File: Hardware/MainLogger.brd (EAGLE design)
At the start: 98.9 x 72.1 mm, 247 parts, among them J3 GEMS_POWER_PLUGINPUT_RT, J4 U.FL, J5 B_SERIES_M.2EKEY_3042, P1:C1 0.1uF, P1:C2 2.2uF, P1:C3 1uF, P1:C4 100uF, P1:C5 0.1uF, P1:J1 CONN_TALON_LOGGER, P1:R1 100k, P1:U1 SN74AUP1G08DCK, P1:U2 FXMAR2102UMLP, P1:U3 FSA2258, P1:U4 AP2411, P2:C1 0.1uF, P2:C2 2.2uF, P2:C3 1uF, P2:C4 100uF, P2:C5 0.1uF, P2:J1 CONN_TALON_LOGGER, P2:R1 100k, P2:U1 SN74AUP1G08DCK, P2:U2 FXMAR2102UMLP, P2:U3 FSA2258, P2:U4 AP2411, P3:C1 0.1uF, P3:C2 2.2uF, P3:C3 1uF, P3:C4 100uF, P3:C5 0.1uF, P3:J1 CONN_TALON_LOGGER, P3:R1 100k, P3:U1 SN74AUP1G08DCK, P3:U2 FXMAR2102UMLP, P3:U3 FSA2258, P3:U4 AP2411, P4:C1 0.1uF, P4:C2 2.2uF, P4:C3 1uF, P4:C4 100uF, P4:C5 0.1uF, P4:J1 CONN_TALON_LOGGER, P4:R1 100k, P4:U1 SN74AUP1G08DCK, P4:U2 FXMAR2102UMLP, P4:U3 FSA2258, P4:U4 AP2411, Q1 DMG3404, Q2 MOSFET_PCH-DMP3036SFG, Q3 MOSFET_PCH-DMP3036SFG, Q4 DMG3404, Q5 NX2301P, Q6 NX2301P, Q7 DMG3404, U1 FXMAR2102UMLP, U10 SIP32431TDFN, U11 LTC4412S6, U12 TCR2LE31ESV, U13 LP59073.3VYKE, U14 MIC22602, U15 BQ25616, U16 TPS61282D, U17 MCP23018QFN, U18 MCP23018QFN, U19 MAX-M8W, U2 VEML3328, U20 MCP79412SOIC, U21 HALL_EFFECT_SI7201, U22 PCA9634QFN, U23 TPL5010DDC, U24 TPL5010DDC, U25 MB85RC, U26 SHTC3DFN, U3 MMC5633, U4 MXC6655, U5 PAC1934QFN, U6 PAC1934QFN, U7 SN74AUP1G08DCK, U8 FXMAR2102UMLP, U9 SN74AUP3G34DCU

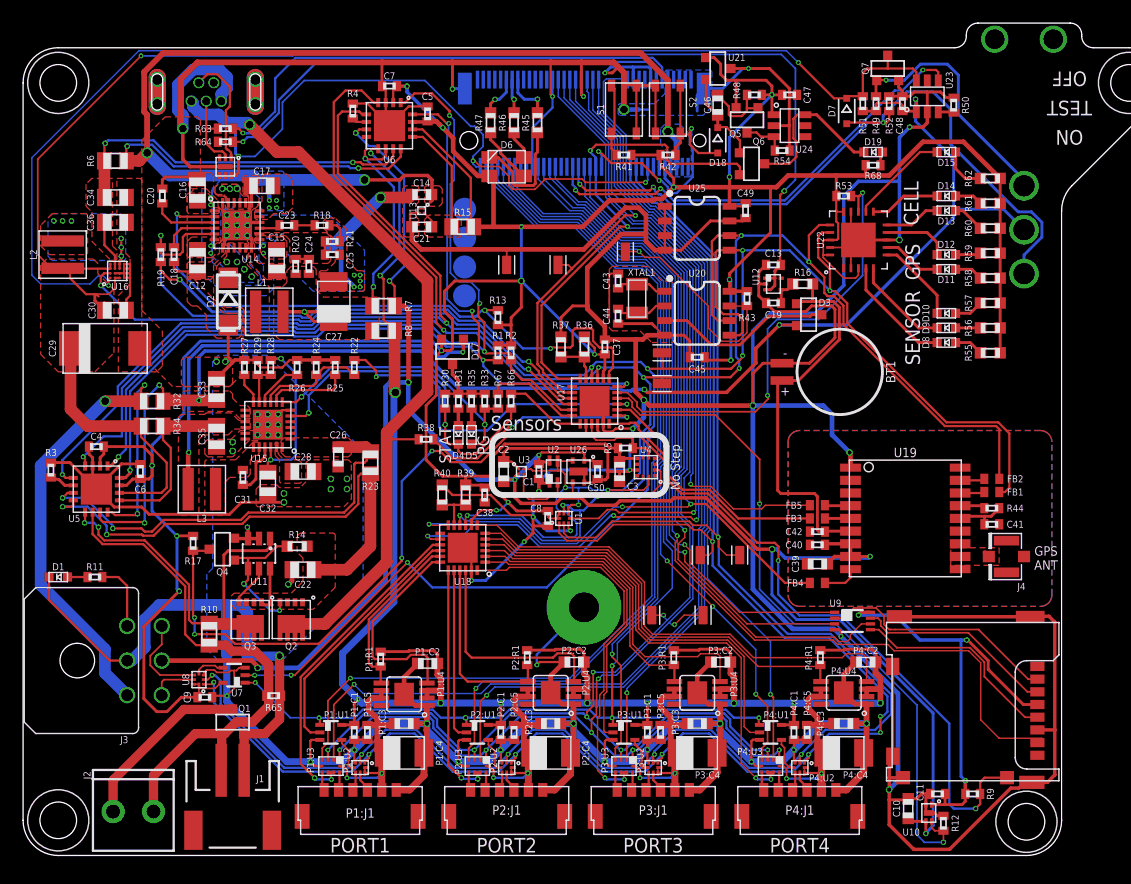
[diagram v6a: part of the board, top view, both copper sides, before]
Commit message: v1.1 Update
Added SIM card, updated pinouts, fixed switch circuit
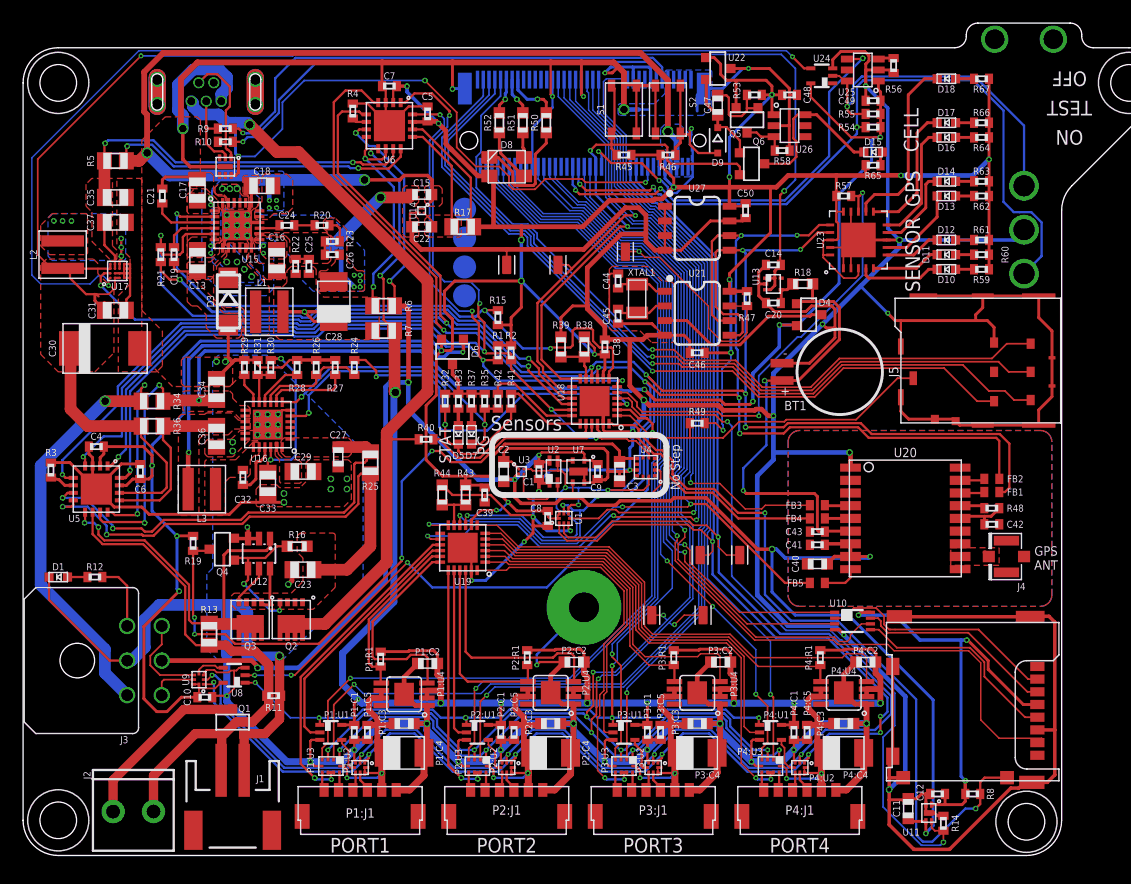
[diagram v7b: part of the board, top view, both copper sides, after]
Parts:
- removed D19: LEDGREEN0603, bschulz:LED_0603
- removed Q7: DMG3404, bschulz:SOT23-3
- removed R68: 10k, bschulz_passives:R0402
- removed TP3, TP4: TESTPOINTRCU, bschulz:TESTPOINT_0603
- added $3_190_$_2021-12-10_02-09-55: B_SERIES_M.2EKEY_3042, Particle-Devices:PARTICLE_M.2EKEY
- added U27: MB85RC, bschulz:SO08
- C10, C14, C39, C46: value 1uF -> 0.1uF; device bschulz_passives:C0603 -> bschulz_passives:C0402
- C11, C40, C47: value 0.1uF -> 1uF; device bschulz_passives:C0402 -> bschulz_passives:C0603
- C12: value 22uF -> 0.1uF; device bschulz_passives:C0805 -> bschulz_passives:C0402
- C13: value 0.1uF -> 22uF; device bschulz_passives:C0402 -> bschulz_passives:C0805
- C15: value 22uF -> 1uF; device bschulz_passives:C0805 -> bschulz_passives:C0603
- C18: value 1nF -> 22uF; device bschulz_passives:C0402 -> bschulz_passives:C0805
- C19: value 0.1uF -> 1nF
- C20: value 10nF -> 0.1uF
- C21: value 1uF -> 10nF; device bschulz_passives:C0603 -> bschulz_passives:C0402
- C22: value 10uF -> 1uF; device bschulz_passives:C0805 -> bschulz_passives:C0603
- C23: value 39pF -> 10uF; device bschulz_passives:C0402 -> bschulz_passives:C0805
- C24: value 10nF -> 39pF
- C25: value 100pF -> 10nF
- C26: value 1uF -> 100pF; device bschulz_passives:C0603 -> bschulz_passives:C0402
- C27: value 100uF -> 1uF; device bschulz_passives:C1411_TANT -> bschulz_passives:C0603
- C28: value 10uF -> 100uF; device bschulz_passives:C0805 -> bschulz_passives:C1411_TANT
- C29: value 220uF -> 10uF; device bschulz_passives:C2917 -> bschulz_passives:C0805
- C30: value 1.5uF -> 220uF; device bschulz_passives:C0805 -> bschulz_passives:C2917
- C31: value 47nF -> 1.5uF; device bschulz_passives:C0402 -> bschulz_passives:C0805
- C32: value 4.7uF -> 47nF; device bschulz_passives:C0805 -> bschulz_passives:C0402
- C33: value 10uF -> 4.7uF
- C37: value 0.1uF -> 10uF; device bschulz_passives:C0402 -> bschulz_passives:C0805
- C41: value 47pF -> 0.1uF
- C42: value 0.1uF -> 47pF
- C43: value 9pF -> 0.1uF
- C45: value 0.1uF -> 9pF
- D10, D15: value LEDRED0603 -> LEDGREEN0603
- D11: value LEDGREEN0603 -> LEDAMBER0603
- D12: value LEDAMBER0603 -> LEDRED0603
- D16: value RCLAMP3654 -> LEDGREEN0603; device bschulz:DFN_6_1.6X1.6 -> bschulz:LED_0603
- D17: value (none) -> LEDAMBER0603; device bschulz:SOT23-3 -> bschulz:LED_0603
- D18: value BAT54WS -> LEDRED0603; device bschulz:SOD323-R -> bschulz:LED_0603
- D2: value CDBA3100 -> RCLAMP3654; device bschulz:DO214AC -> bschulz:DFN_6_1.6X1.6
- D3: value BAT54C -> CDBA3100; device bschulz:SOT23-3 -> bschulz:DO214AC
- D4: value LEDGREEN0603 -> BAT54C; device bschulz:LED_0603 -> bschulz:SOT23-3
- D5: value LEDAMBER0603 -> LEDGREEN0603
- D6: value CLVBA-FKA -> (none); device bschulz:CLVBA-FKA -> bschulz:SOT23-3
- D7: value BAT54WS -> LEDAMBER0603; device bschulz:SOD323-R -> bschulz:LED_0603
- D8: value LEDGREEN0603 -> CLVBA-FKA; device bschulz:LED_0603 -> bschulz:CLVBA-FKA
- D9: value LEDAMBER0603 -> BAT54WS; device bschulz:LED_0603 -> bschulz:SOD323-R
- J5: value B_SERIES_M.2EKEY_3042 -> SIM_CDNANO_SF72; device Particle-Devices:PARTICLE_M.2EKEY -> bschulz:SIM_SF72
- R10: value 2m -> 27R; device bschulz_passives:R0805 -> bschulz_passives:R0402
- R11: value 1k -> 1M
- R12: value 100k -> 1k
- R13: value 100k -> 2m; device bschulz_passives:R0402 -> bschulz_passives:R0805
- R14: value 470k -> 100k; device bschulz_passives:R0603 -> bschulz_passives:R0402
- R15: value 10m -> 100k; device bschulz_passives:R0805 -> bschulz_passives:R0402
- R16: value 1k -> 470k
- R17: value 1M -> 10m; device bschulz_passives:R0402 -> bschulz_passives:R0805
- R18: value 20k -> 1k; device bschulz_passives:R0402 -> bschulz_passives:R0603
- R19: value 100k -> 1M
- R20: value 10k -> 20k
- R21: value 2.7k -> 100k
- R22: value 0R -> 10k
- R23: value 2m -> 2.7k; device bschulz_passives:R0805 -> bschulz_passives:R0402
- R24: value 1M -> 0R
- R25: value 470R -> 2m; device bschulz_passives:R0402 -> bschulz_passives:R0805
- R26: value 220R -> 1M
- R27: value 10k -> 470R
- R28: value 100k -> 220R
- R29: value 100k -> 10k
- R30: value 1M -> 100k
- R31: value 10k -> 100k
- R32: value 10m -> 1M; device bschulz_passives:R0805 -> bschulz_passives:R0402
- R33, R65: value 1M -> 10k
- R35, R41, R42, R54: value 10k -> 1M
- R36: value 150k -> 10m; device bschulz_passives:R0603 -> bschulz_passives:R0805
- R37, R59, R60, R61, R62: device bschulz_passives:R0603 -> bschulz_passives:R0402
- R38: value 1M -> 150k; device bschulz_passives:R0402 -> bschulz_passives:R0603
- R39: value 130k -> 10k
- R40: value 30k -> 1M; device bschulz_passives:R0603 -> bschulz_passives:R0402
- R43: value 100k -> 130k; device bschulz_passives:R0402 -> bschulz_passives:R0603
- R44: value 10 -> 30k; device bschulz_passives:R0402 -> bschulz_passives:R0603
- R45, R46: value 4.7k -> 10k; device bschulz_passives:R0603 -> bschulz_passives:R0402
- R47: value 4.7k -> 100k; device bschulz_passives:R0603 -> bschulz_passives:R0402
- R48: value 100k -> 10
- R49: value 1M -> (none)
- R5: value 10k -> 2m; device bschulz_passives:R0402 -> bschulz_passives:R0805
- R50: value 100k -> 4.7k; device bschulz_passives:R0402 -> bschulz_passives:R0603
- R51, R52: value 1M -> 4.7k; device bschulz_passives:R0402 -> bschulz_passives:R0603
- R55: value 220R -> 1M; device bschulz_passives:R0603 -> bschulz_passives:R0402
- R56, R57: value 220R -> 100k; device bschulz_passives:R0603 -> bschulz_passives:R0402
- R58: value 220R -> 10k; device bschulz_passives:R0603 -> bschulz_passives:R0402
- R63, R64: value 27R -> 220R
- R66, R67: value 1M -> 220R
- R8: value 2m -> 100k; device bschulz_passives:R0805 -> bschulz_passives:R0402
- R9: value 100k -> 27R
- U10: value SIP32431TDFN -> SN74AUP3G34DCU; device bschulz:TDFN_4 -> bschulz:DCU_(R-PDSO-G8)
- U11: value LTC4412S6 -> SIP32431TDFN; device bschulz:SOT23-6L -> bschulz:TDFN_4
- U12: value TCR2LE31ESV -> LTC4412S6; device bschulz:SOT-553 -> bschulz:SOT23-6L
- U13: value LP59073.3VYKE -> TCR2LE31ESV; device bschulz:YKE0004 -> bschulz:SOT-553
- U14: value MIC22602 -> LP59073.3VYKE; device bschulz:QFN24_POWER -> bschulz:YKE0004
- U15: value BQ25616 -> MIC22602
- U16: value TPS61282D -> BQ25616; device bschulz:YFP0016 -> bschulz:QFN24_POWER
- U17: value MCP23018QFN -> TPS61282D; device bschulz:QFN24 -> bschulz:YFP0016
- U19: value MAX-M8W -> MCP23018QFN; device bschulz:MAX-M8 -> bschulz:QFN24
- U20: value MCP79412SOIC -> MAX-M8W; device bschulz:SO08 -> bschulz:MAX-M8
- U21: value HALL_EFFECT_SI7201 -> MCP79412SOIC; device bschulz:SOT23-3 -> bschulz:SO08
- U22: value PCA9634QFN -> HALL_EFFECT_SI7201; device bschulz:QFN20_5X5 -> bschulz:SOT23-3
- U23: value TPL5010DDC -> PCA9634QFN; device bschulz:DDC_R-PDSO-G6 -> bschulz:QFN20_5X5
- U24: value TPL5010DDC -> SN74LVC1G17DCK; device bschulz:DDC_R-PDSO-G6 -> bschulz:DCK_R-PDSO-G5
- U25: value MB85RC -> TPL5010DDC; device bschulz:SO08 -> bschulz:DDC_R-PDSO-G6
- U26: value SHTC3DFN -> TPL5010DDC; device bschulz:DFN_4_2X2 -> bschulz:DDC_R-PDSO-G6
- U7: value SN74AUP1G08DCK -> SHTC3DFN; device bschulz:DCK_R-PDSO-G5 -> bschulz:DFN_4_2X2
- U8: value FXMAR2102UMLP -> SN74AUP1G08DCK; device bschulz:UQFN-8_1.4X1.2 -> bschulz:DCK_R-PDSO-G5
- U9: value SN74AUP3G34DCU -> FXMAR2102UMLP; device bschulz:DCU_(R-PDSO-G8) -> bschulz:UQFN-8_1.4X1.2
- moved R9 86.7 mm to (17.5, 63.0)
- moved C12 79.1 mm to (79.2, 5.33), turned to 180 degrees
- moved R12 76.6 mm to (6.22, 24.1), turned to 180 degrees
- moved R65 69.4 mm to (73.7, 59.8)
- moved R63 65.7 mm to (83.1, 58.4), turned to 0 degrees
- moved R64 65.5 mm to (83.1, 62.2), turned to 0 degrees
- moved R8 64.9 mm to (82.3, 5.33)
- moved D16 62.5 mm to (80.0, 62.2), turned to 0 degrees
- moved U11 62.2 mm to (78.5, 3.68), turned to 270 degrees
- moved C10 61.7 mm to (15.7, 13.7), turned to 0 degrees
- moved R14 60.9 mm to (79.8, 2.79), turned to 270 degrees
- moved U9 56.9 mm to (15.2, 15.2), turned to 90 degrees
- moved C20 53.8 mm to (65.0, 47.9), turned to 180 degrees
- moved C19 52.1 mm to (13.1, 52.1), turned to 270 degrees
- moved R5 50.7 mm to (8.00, 60.2)
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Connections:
- removed net ACCEL_INT: R5.1, U17.21, U4.5
- removed net CSA_ALERT: R2.1, U17.17, U5.1, U6.1
- removed net N$15: R38.1, U17.1
- new net EN_MAIN_OD: R55.2, S3.1, U24.2, U25.6
- new net SENSOR_INT: R2.1, U18.17, U4.5, U5.1, U6.1
- new net SIM_CD: J5.DSW, R49.1, U18.1
- new net SIM_CLK: $3_190_$_2021-12-10_02-09-55.71, J5.3
- new net SIM_DATA: $3_190_$_2021-12-10_02-09-55.73, J5.7
- new net SIM_RST: $3_190_$_2021-12-10_02-09-55.69, J5.2
- new net UB_VBUS: $3_190_$_2021-12-10_02-09-55.74
- new net VPP: J5.6
- net !CE: now also R24.1, U18.3; no longer R22.1, U17.3
- net !CHG_PG: now also D7.CATHODE, R35.1, R42.2, U16.7; no longer D5.CATHODE, R33.1, R67.2, U15.7
- net !MODE: now also $3_190_$_2021-12-10_02-09-55.32, D9.A, R46.1; no longer D18.A, J5.32, R42.1
- net !RESET: now also $3_190_$_2021-12-10_02-09-55.34, FB5.2, R45.1, U19.12; no longer FB4.2, J5.34, R41.1, U17.12
- net !TALON1_FAULT: now also U19.17; no longer U18.17
- net !TALON2_FAULT: now also U19.21; no longer U18.21
- net !TALON3_FAULT: now also U19.2; no longer U18.2
- net !TALON4_FAULT: now also U19.6; no longer U18.6
- net 3V3_AUX: now also C11.1, C41.1, C9.1, R6.1, U11.3, U20.7, U20.8, U7.1; no longer C10.1, C39.1, C50.1, R7.1, U10.3, U19.7, U19.8, U26.1
- net 3V3_AUX_EN: now also R15.1, U15.2, U18.7; no longer R13.1, U14.2, U17.7
- net 3V3_AUX_PG: now also R21.1, U15.5, U18.15; no longer R19.1, U14.5, U17.15
- net 3V3_BULK: now also R7.1; no longer R8.1
- net 3V3_BULK+: now also C25.1, C28.ANODE, R21.2, R22.2, R6.2; no longer C24.1, C27.ANODE, R19.2, R20.2, R8.2
- net 3V3_CORE: now also $3_190_$_2021-12-10_02-09-55.10, $3_190_$_2021-12-10_02-09-55.12, C10.1, C39.1, C46.1, C48.1, C50.1, D8.2, R19.2, R38.2, R45.2, R46.2, R47.2, R49.2, R63.2, R64.2, R65.2, R66.2, R67.2, U19.8, U21.8, U22.1, U23.15, U23.18, U23.20, U23.3, U26.1, U27.8, U8.5, U9.1, U9.8; no longer C37.1, C45.1, C47.1, C49.1, C9.1, D17.2, J5.10, J5.12, R13.2, R36.2, R39.2, R41.2, R42.2, R48.2, R5.2, R55.2, R56.2, R58.2, R68.2, U17.8, U20.8, U21.1, U22.15, U22.18, U22.20, U22.3, U24.1, U25.8, U7.5, U8.1, U8.8
- net 3V3_CORE+: now also C22.1, R17.1, U14.A2; no longer C21.1, R15.1, U13.A2
- net 3V3_SD: now also C12.1, R8.2, U10.8, U11.1; no longer C11.1, R9.2, U10.1, U9.8
- net 3V3_SD_EN: now also R14.2, U11.4, U18.4; no longer R12.2, U10.4, U17.4
- net BAT: now also R34.2; no longer R32.2
- net BAT_CHG: now also C34.1, C49.1, D4.2, R34.1, R54.1, R55.1, U16.13, U16.14, U24.5, U25.1; no longer C33.1, C48.1, D3.2, R32.1, R49.1, R51.2, S3.2, U15.13, U15.14, U23.1
- net BCKP_GPS: now also C43.1, D4.1, R18.2, U20.6; no longer C42.1, D3.1, R16.2, U19.6
- net BCKP_RTC: now also D4.3, U21.3; no longer D3.3, U20.3
- net BTST: now also C32.2, U16.21; no longer C31.2, U15.21
- net CHG_SOURCE: now also R19.1, U18.21; no longer R17.1, U17.20
- net CHG_STAT: now also D5.CATHODE, R32.1, R41.2, U16.5; no longer D4.CATHODE, R30.1, R66.2, U15.5
- net COMP: now also C24.1, U15.15; no longer C23.1, U14.15
- net CSA_EN: now also U18.6; no longer U17.6
- net D+: now also $3_190_$_2021-12-10_02-09-55.11, R9.1; no longer J5.11, R63.1
- net D+_IN: now also D2.2, R9.2; no longer D16.2, R63.2
- net D-: now also $3_190_$_2021-12-10_02-09-55.13, R10.1; no longer J5.13, R64.1
- net D-_IN: now also D2.1, R10.2; no longer D16.1, R64.2
- net DELAY: now also C21.1, U15.3; no longer C20.1, U14.3
- net EN_MAIN: now also U17.A1, U24.4; no longer D7.C, Q7.3, R51.1, U16.A1, U23.6
- net FAULT_BUS: now also R12.2; no longer R11.2
- net FB: now also C25.2, C26.1, R22.1, R23.2, U15.14; no longer C24.2, C25.1, R20.1, R21.2, U14.14
- net GND: now also $3_190_$_2021-12-10_02-09-55.1, $3_190_$_2021-12-10_02-09-55.15, $3_190_$_2021-12-10_02-09-55.21, $3_190_$_2021-12-10_02-09-55.3, $3_190_$_2021-12-10_02-09-55.39, $3_190_$_2021-12-10_02-09-55.49, $3_190_$_2021-12-10_02-09-55.5, $3_190_$_2021-12-10_02-09-55.56, $3_190_$_2021-12-10_02-09-55.7, $3_190_$_2021-12-10_02-09-55.76, $3_190_$_2021-12-10_02-09-55.77, $3_190_$_2021-12-10_02-09-55.9, $3_190_$_2021-12-10_02-09-55.GND, C23.2, C27.2, C28.CATHODE, C29.2, C30.-, C31.2, C46.2, D2.EP, D3.A, J5.CSW, J5.GND@1, J5.GND@10, J5.GND@2, J5.GND@3, J5.GND@4, J5.GND@5, J5.GND@6, J5.GND@7, J5.GND@8, J5.GND@9, R11.1, R14.1, R20.1, R23.1, R27.1, R28.1, R29.2, R31.1, R39.1, R44.1, R56.1, R58.1, S3.2, U10.4, U11.EP, U12.3, U13.2, U14.B2, U15.12, U15.16, U15.19, U15.24, U15.7, U16.17, U16.18, U16.6, U16.EP, U16.EP@1, U16.EP@2, U16.EP@3, U16.EP@4, U16.EP@5, U16.EP@6, U16.EP@7, U16.EP@8, U16.EP@9, U17.B2, U17.C2, U17.D1, U17.D2, U17.D3, U17.D4, U19.23, U19.EP, U20.1, U20.10, U20.12, U21.4, U22.3, U23.1, U23.14, U23.19, U23.8, U23.EP, U24.3, U26.2, U27.1, U27.2, U27.3, U27.4, U27.7, U7.4, U7.EP, U8.3; no longer C25.2, C27.CATHODE, C28.2, C29.-, C30.2, C32.2, C47.2, D16.EP, D2.A, J5.1, J5.15, J5.21, J5.3, J5.39, J5.49, J5.56, J5.7, J5.76, J5.77, J5.9, J5.GND, Q7.2, R12.1, R18.1, R21.1, R24.1, R25.1, R27.2, R29.1, R37.1, R40.1, R50.1, R52.1, R54.1, R65.1, U10.2, U10.EP, U11.3, U13.B2, U14.12, U14.16, U14.19, U14.24, U14.7, U14.EP, U14.EP@1, U14.EP@2, U14.EP@3, U14.EP@4, U14.EP@5, U14.EP@6, U14.EP@7, U14.EP@8, U14.EP@9, U15.17, U15.18, U15.6, U16.B2, U16.C2, U16.D1, U16.D2, U16.D3, U16.D4, U17.23, U17.EP, U19.1, U19.10, U19.12, U20.4, U21.3, U22.1, U22.14, U22.19, U22.2, U22.8, U22.EP, U24.2, U25.1, U25.3, U25.4, U25.7, U26.4, U26.EP, U7.3, U8.4
- net GPS_ANT: now also U20.11; no longer U19.11
- net GPS_INT: now also FB4.1, U18.22; no longer FB3.1, U17.24
- net GPS_INT_CLEAN: now also FB4.2, U20.5; no longer FB3.2, U19.5
- net I2C_EXT_EN: now also U18.2, U8.2; no longer U17.2, U7.2
- net I2C_EXT_EN_OUT: now also U8.4, U9.5; no longer U7.4, U8.5
- net I2C_GLOBAL_EN: now also $3_190_$_2021-12-10_02-09-55.64, U8.1; no longer J5.64, U7.1
- net I2C_OB_EN: now also $3_190_$_2021-12-10_02-09-55.45; no longer J5.45
- net ICHG: now also R28.2, U16.10; no longer R26.2, U15.10
- net ILIM: now also R27.2, U16.8; no longer R25.2, U15.8
- net LED_BLUE: now also $3_190_$_2021-12-10_02-09-55.65, R52.2; no longer J5.65, R47.2
- net LED_EN: now also R57.1, U18.5, U23.13; no longer R53.1, U17.5, U22.13
- net LED_GREEN: now also $3_190_$_2021-12-10_02-09-55.63, R51.2; no longer J5.63, R46.2
- net LED_RED: now also $3_190_$_2021-12-10_02-09-55.61, R50.2; no longer J5.61, R45.2
- net MISO: now also $3_190_$_2021-12-10_02-09-55.50; no longer J5.50
- net MOSI: now also $3_190_$_2021-12-10_02-09-55.52, U10.1; no longer J5.52, U9.1
- net MOSI_BUF: now also U10.7; no longer U9.7
- net N$10: now also R26.2, U16.9; no longer R22.2, U15.9
- net N$11: now also C47.1, D9.C, U22.2; no longer C46.1, D18.C, U21.2
- net N$12: now also D15.CATHODE, U26.6; no longer D19.CATHODE, U24.6
- net N$13: now also C47.2, R53.1; no longer C46.2, R48.1
- net N$14: now also D15.ANODE, R65.1; no longer D19.ANODE, R68.1
- net N$18: now also D7.ANODE, R37.1; no longer D5.ANODE, R35.1
- net N$20: now also D5.ANODE, R33.1; no longer D4.ANODE, R31.1
- net N$21: now also D8.3, R52.1; no longer D6.3, R47.1
- net N$22: now also D8.4, R51.1; no longer D6.4, R46.1
- net N$23: now also D8.1, R50.1; no longer D6.1, R45.1
- net N$24: now also FB5.1, U20.9; no longer FB4.1, U19.9
- net N$25: now also R12.1; no longer R11.1
- net N$3: now also C20.1, R18.1, U13.4; no longer C19.1, R16.1, U12.4
- net N$30: now also R56.2, U25.3; no longer R50.2, U23.3
- net N$32: now also R58.2, U26.3; no longer R54.2, U24.3
- net N$33: now also C24.2, R20.2; no longer C23.2, R18.2
- net N$35: now also R43.1, R44.2, U19.11; no longer R39.1, R40.2, U18.11
- net N$36: now also D10.CATHODE, U23.4; no longer D8.CATHODE, U22.4
- net N$37: now also D11.CATHODE, U23.5; no longer D9.CATHODE, U22.5
- net N$38: now also R38.1, R39.2, U18.11; no longer R36.1, R37.2, U17.11
- net N$39: now also D12.CATHODE, U23.6; no longer D10.CATHODE, U22.6
- net N$4: now also C44.1, U21.1; no longer C43.1, U20.1
- net N$40: now also D13.CATHODE, U23.7; no longer D11.CATHODE, U22.7
- net N$41: now also D14.CATHODE, U23.9; no longer D12.CATHODE, U22.9
- net N$42: now also D16.CATHODE, U23.10; no longer D13.CATHODE, U22.10
- net N$43: now also D17.CATHODE, U23.11; no longer D14.CATHODE, U22.11
- net N$44: now also D18.CATHODE, U23.12; no longer D15.CATHODE, U22.12
- net N$45: now also D10.ANODE, R59.1; no longer D8.ANODE, R55.1
- net N$46: now also D11.ANODE, R60.1; no longer D9.ANODE, R56.1
- net N$47: now also D12.ANODE, R61.1; no longer D10.ANODE, R57.1
- net N$48: now also D13.ANODE, R62.1; no longer D11.ANODE, R58.1
- net N$49: now also D14.ANODE, R63.1; no longer D12.ANODE, R59.1
- net N$5: now also U12.5; no longer U11.5
- net N$50: now also D16.ANODE, R64.1; no longer D13.ANODE, R60.1
- net N$51: now also D17.ANODE, R66.1; no longer D14.ANODE, R61.1
- net N$52: now also D18.ANODE, R67.1; no longer D15.ANODE, R62.1
- net N$6: now also R41.1, U18.19; no longer R66.1, U17.19
- net N$7: now also C45.1, U21.2; no longer C44.1, U20.2
- net N$8: now also R40.1, U18.20; no longer Q7.1, R49.2, S3.1
- net N$9: now also R42.1, U18.18; no longer R67.1, U17.18
- net OB_INT: now also $3_190_$_2021-12-10_02-09-55.43, U18.14; no longer J5.43, U17.14
- net PMID: now also C29.1, U16.23; no longer C28.1, U15.23
- net RC: now also C19.1, U15.4; no longer C18.1, U14.4
- net REGN: now also C33.1, R30.2, U16.22; no longer C32.1, R28.2, U15.22
- net RTC_INT: now also $3_190_$_2021-12-10_02-09-55.62, R47.1, U21.7; no longer J5.62, R43.1, U20.7
- net RX: now also $3_190_$_2021-12-10_02-09-55.38; no longer J5.38
- net SCK: now also $3_190_$_2021-12-10_02-09-55.54, U10.3; no longer J5.54, U9.3
- net SCK_BUF: now also U10.5; no longer U9.5
- net SCL: now also $3_190_$_2021-12-10_02-09-55.20, U9.3; no longer J5.20, U8.3
- net SCL_EXT: now also U9.6; no longer U8.6
- net SCL_GPS: now also U20.17; no longer U19.17
- net SCL_OB: now also U19.9, U21.6, U23.16, U27.6, U7.2; no longer TP4.1, U17.9, U20.6, U22.16, U25.6, U26.2
- net SDA: now also $3_190_$_2021-12-10_02-09-55.22, U9.2; no longer J5.22, U8.2
- net SDA_EXT: now also U9.7; no longer U8.7
- net SDA_GPS: now also U20.16; no longer U19.16
- net SDA_OB: now also U19.10, U21.5, U23.17, U27.5, U7.3; no longer TP3.1, U17.10, U20.5, U22.17, U25.5, U26.3
- net SD_CD: now also R8.1, U18.24; no longer R9.1, U17.22
- net SD_CS: now also $3_190_$_2021-12-10_02-09-55.48, U10.6; no longer J5.48, U9.6
- net SD_CS_BUF: now also U10.2; no longer U9.2
- net SIM_VCC: now also $3_190_$_2021-12-10_02-09-55.67, J5.1; no longer J5.67
- net SOLAR+: now also R11.2, R13.1; no longer R10.1, R65.2
- net STAT_CORE: now also D6.3, R32.2, R37.2; no longer D17.3, R30.2, R31.2
- net ST_CORE: now also R16.1, U12.4; no longer R14.1, U11.4
- net SW: now also C32.1, U16.19, U16.20; no longer C31.1, U15.19, U15.20
- net SW1: now also D3.C, U15.10, U15.11, U15.20, U15.21, U15.22, U15.23, U15.8, U15.9; no longer D2.C, U14.10, U14.11, U14.20, U14.21, U14.22, U14.23, U14.8, U14.9
- net SW2: now also U17.C3, U17.C4; no longer U16.C3, U16.C4
- net SYS: now also C14.1, C30.+, C31.1, R36.2, U13.1, U13.3, U17.A3, U17.A4, U17.B1, U17.C1; no longer C13.1, C29.+, C30.1, R34.2, U12.1, U12.3, U16.A3, U16.A4, U16.B1, U16.C1
- net SYSCORE: now also C36.1, D6.1, R36.1, U16.15, U16.16; no longer C35.1, D17.1, R34.1, U15.15, U15.16
- net TALON1_EN: now also U19.18; no longer U18.18
- net TALON1_GPIOA: now also $3_190_$_2021-12-10_02-09-55.37; no longer J5.37
- net TALON1_GPIOB: now also $3_190_$_2021-12-10_02-09-55.72; no longer J5.72
- net TALON1_I2C_EN: now also U19.16; no longer U18.16
- net TALON1_SEL: now also U19.15; no longer U18.15
- net TALON2_EN: now also U19.22; no longer U18.22
- net TALON2_GPIOA: now also $3_190_$_2021-12-10_02-09-55.35; no longer J5.35
- net TALON2_GPIOB: now also $3_190_$_2021-12-10_02-09-55.70; no longer J5.70
- net TALON2_I2C_EN: now also U19.20; no longer U18.20
- net TALON2_SEL: now also U19.19; no longer U18.19
- net TALON3_EN: now also U19.3; no longer U18.3
- net TALON3_GPIOA: now also $3_190_$_2021-12-10_02-09-55.33; no longer J5.33
- net TALON3_GPIOB: now also $3_190_$_2021-12-10_02-09-55.68; no longer J5.68
- net TALON3_I2C_EN: now also U19.1; no longer U18.1
- net TALON3_SEL: now also U19.24; no longer U18.24
- net TALON4_EN: now also U19.7; no longer U18.7
- net TALON4_GPIOA: now also $3_190_$_2021-12-10_02-09-55.23; no longer J5.23
- net TALON4_GPIOB: now also $3_190_$_2021-12-10_02-09-55.66; no longer J5.66
- net TALON4_I2C_EN: now also U19.5; no longer U18.5
- net TALON4_SEL: now also U19.4; no longer U18.4
- net TALON_INT: now also $3_190_$_2021-12-10_02-09-55.41, U19.14; no longer J5.41, U18.14
- net TEST: now also $3_190_$_2021-12-10_02-09-55.40, R54.2; no longer D7.A, J5.40, R52.2
- net TIMEPULSE: now also $3_190_$_2021-12-10_02-09-55.47, FB3.1; no longer FB5.1, J5.47
- net TIMEPULSE_CLEAN: now also FB3.2, U20.4; no longer FB5.2, U19.4
- net TS: now also R30.1, R31.2, U16.11; no longer R28.1, R29.2, U15.11
- net TX: now also $3_190_$_2021-12-10_02-09-55.36; no longer J5.36
- net VBULK: now also $3_190_$_2021-12-10_02-09-55.2, $3_190_$_2021-12-10_02-09-55.4, $3_190_$_2021-12-10_02-09-55.6, $3_190_$_2021-12-10_02-09-55.8, C13.1, C18.1, R5.1, U14.A1, U14.B1, U15.1, U15.13, U15.17, U15.18, U15.6; no longer C12.1, C14.1, J5.2, J5.4, J5.6, J5.8, R6.1, U13.A1, U13.B1, U14.1, U14.13, U14.17, U14.18, U14.6
- net VBULK+: now also C35.1, C37.1, R5.2, U17.B3, U17.B4; no longer C34.1, C36.1, R6.2, U16.B3, U16.B4
- net VBULK_PG: now also U17.A2, U18.16; no longer U16.A2, U17.16
- net VBUS: now also C27.1, R25.2, U16.1, U16.24; no longer C26.1, R23.2, U15.1, U15.24
- net VCC_RF: now also C42.1, R48.1, U20.14; no longer C41.1, R44.1, U19.14
- net VPRIME: now also C23.1, R16.2, R25.1, U12.6; no longer C22.1, R14.2, R23.1, U11.6
- net VSET: now also R29.1, U16.12; no longer R27.1, U15.12
- net VSOLAR: now also R13.2, U12.1; no longer R10.2, U11.1
- net VUSB: now also $3_190_$_2021-12-10_02-09-55.16, D2.6, R40.2; no longer D16.6, J5.16, J5.74, R38.2
- net V_ANT: now also R48.2, U20.15; no longer R44.2, U19.15
- net WDT_DONE: now also $3_190_$_2021-12-10_02-09-55.42, U25.4; no longer J5.42, U23.4
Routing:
- net SENSOR_INT: track 0.00 -> 92.7 mm, vias 0 -> 6
- net CSA_ALERT: track 80.6 -> 0.00 mm, vias 4 -> 0
- net SIM_CLK: track 0.00 -> 70.7 mm, vias 0 -> 1
- net SIM_RST: track 0.00 -> 69.4 mm, vias 0 -> 1
- net SIM_DATA: track 0.00 -> 67.8 mm, vias 0 -> 1
- net SIM_VCC: track 0.00 -> 67.3 mm, vias 0 -> 1
- net GND: track 847.0 -> 901.8 mm, vias 54 -> 56
- net SIM_CD: track 0.00 -> 30.0 mm
- net EN_MAIN_OD: track 0.00 -> 29.9 mm, vias 0 -> 1
- net N$15: track 19.8 -> 0.00 mm, vias 2 -> 0
- net EN_MAIN: track 105.2 -> 90.7 mm
- net ACCEL_INT: track 7.74 -> 0.00 mm
- net N$44: track 8.60 -> 15.9 mm
- net BAT_CHG: track 128.3 -> 121.5 mm, vias 6 -> 7
- net 3V3_CORE: track 336.8 -> 342.9 mm, vias 16 -> 19
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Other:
- board text added: "Battery"
- board text added: "Ext SIM"
- board text added: "Project Kestrel v1.1 Bobby Schulz"
- board text added: "uSD Card"
- board text removed: "Project Kestrel v1.0 Bobby Schulz"
- board text removed: "SCL_OB"
- board text removed: "SDA_OB"

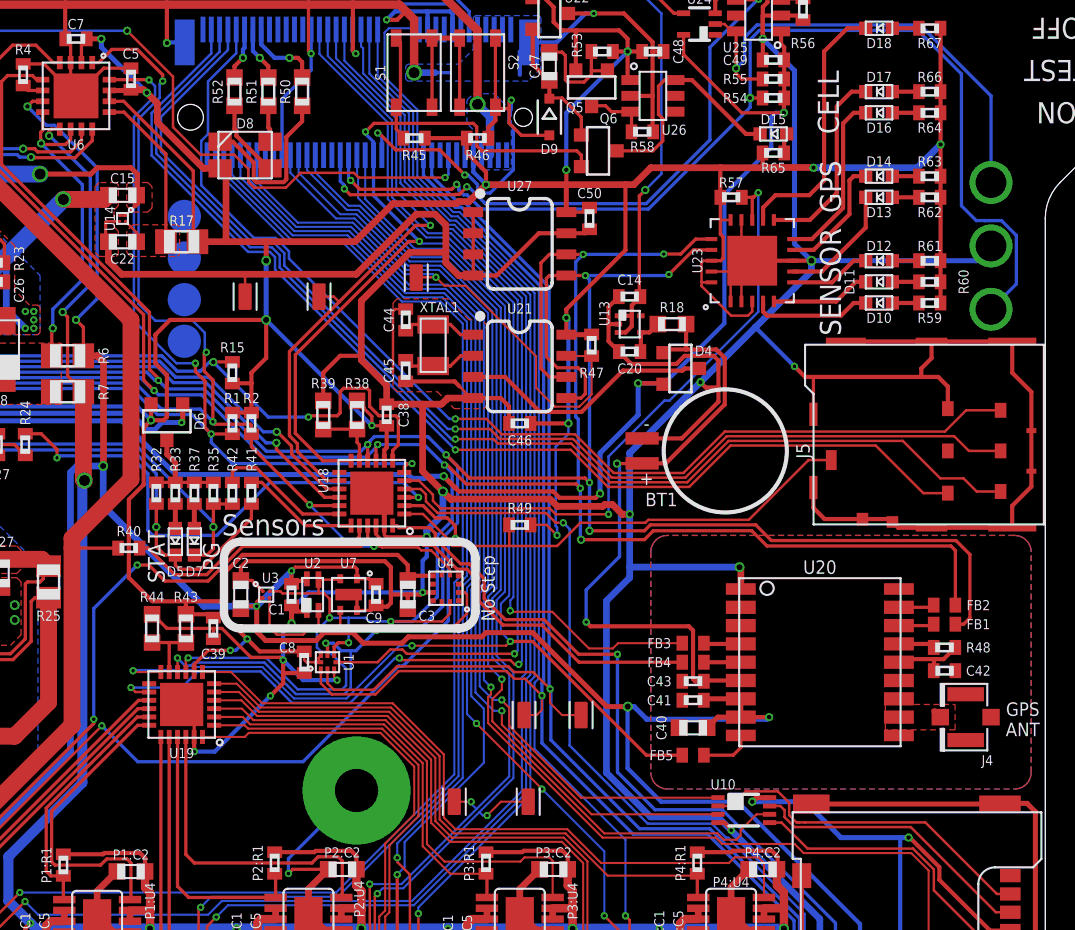
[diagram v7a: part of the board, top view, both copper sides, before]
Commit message: v1.2 Updates
Added I2C_AUX buffer, switched SHT31 to SHT41
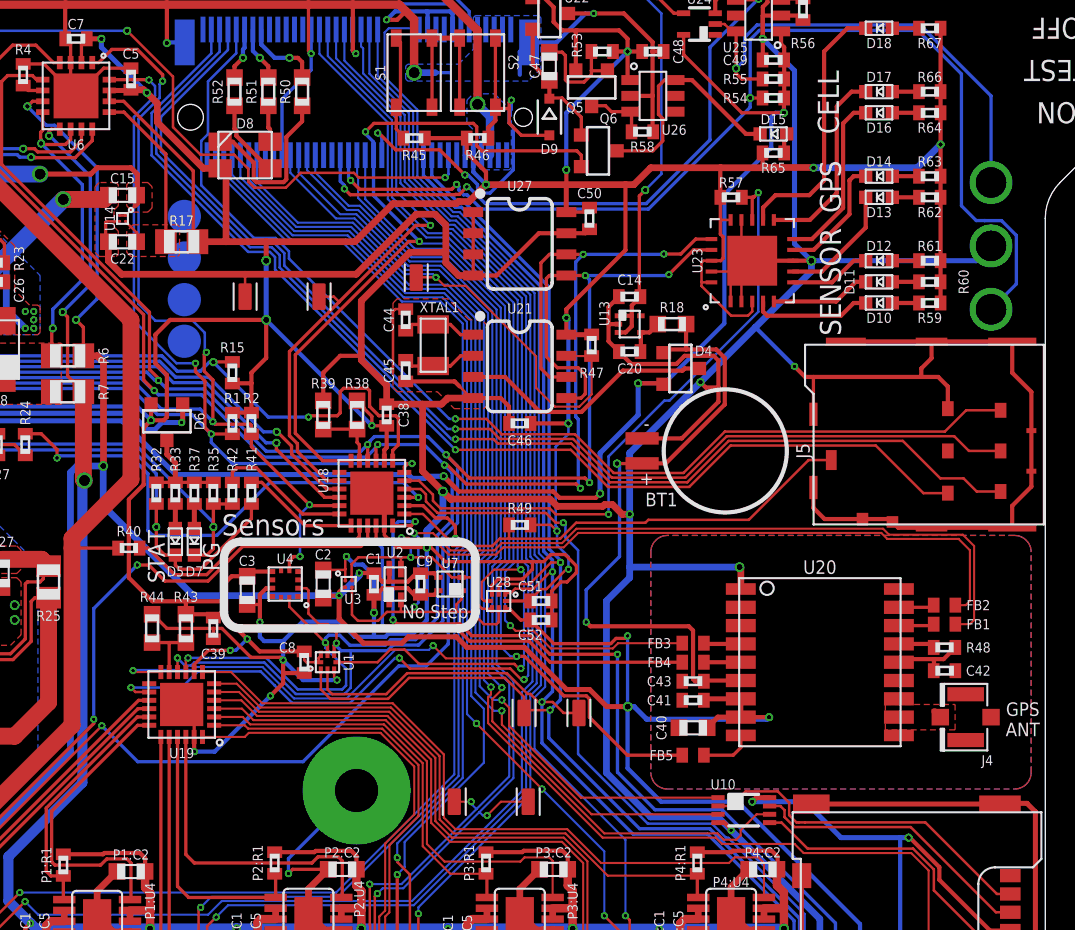
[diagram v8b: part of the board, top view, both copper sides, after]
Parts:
- added C51, C52: 0.1uF, bschulz_passives:C0402
- added U28: FXMAR2102UMLP, bschulz:UQFN-8_1.4X1.2
- U7: value SHTC3DFN -> SHT40; device bschulz:DFN_4_2X2 -> bschulz:SHT4X
- moved C3 9.66 mm to (42.0, 33.5)
- moved U4 9.66 mm to (44.3, 33.9)
- moved U7 6.13 mm to (54.2, 33.9), turned to 180 degrees
- moved C2 4.99 mm to (46.6, 33.9)
- moved U2 4.99 mm to (50.9, 33.9)
- moved U3 4.99 mm to (48.1, 33.9)
- moved C1 4.99 mm to (49.7, 33.9)
- moved TP6 3.43 mm to (58.7, 26.2)
- moved TP5 3.30 mm to (62.0, 26.2)
- moved C9 2.74 mm to (52.5, 33.9)
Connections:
- new net SCL_AUX: FB2.1, U2.3, U28.6, U3.A2, U7.2
- new net SDA_AUX: FB1.1, U2.2, U28.7, U3.B2, U7.1
- net 3V3_AUX: now also C52.1, U28.8, U7.3; no longer U7.1
- net 3V3_CORE: now also C51.1, U28.1
- net GND: now also C51.2, C52.2, U28.4; no longer U7.EP
- net I2C_OB_EN: now also U28.5
- net SCL: now also U1.2, U28.3; no longer U1.3
- net SCL_OB: now also U1.7; no longer FB2.1, U1.6, U2.3, U3.A2, U7.2
- net SDA: now also U1.3, U28.2; no longer U1.2
- net SDA_OB: now also U1.6; no longer FB1.1, U1.7, U2.2, U3.B2, U7.3
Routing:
- net SDA_AUX: track 0.00 -> 59.9 mm, vias 0 -> 2
- net SCL_AUX: track 0.00 -> 53.3 mm, vias 0 -> 2
- net SDA_OB: track 213.0 -> 168.2 mm, vias 11 -> 9
- net SCL_OB: track 207.7 -> 167.8 mm, vias 12 -> 9
- net GND: track 901.8 -> 918.3 mm, vias 56 -> 57
- net 3V3_AUX: track 173.7 -> 183.3 mm, vias 9 -> 10
- net I2C_OB_EN: track 54.2 -> 60.2 mm, vias 1 -> 2
- net SENSOR_INT: track 92.7 -> 86.9 mm
- net SD_CD: track 64.8 -> 70.1 mm, vias 2 -> 4
- net 3V3_CORE: track 342.9 -> 337.9 mm, vias 19 -> 20
- net SDA: track 155.1 -> 159.2 mm, vias 8 -> 9
- net SCL: track 155.2 -> 159.2 mm, vias 6 -> 7
- net GPS_INT: track 22.8 -> 25.2 mm, vias 0 -> 2
- net !RESET: track 116.2 -> 118.0 mm
- net TALON_INT: track 69.8 -> 71.6 mm
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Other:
- board text added: "Project Kestrel v1.2 Bobby Schulz"
- board text removed: "Project Kestrel v1.1 Bobby Schulz"
